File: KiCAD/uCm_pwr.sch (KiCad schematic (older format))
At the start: 31 parts, among them J1 5V_EXT, J2 3V3_EXT, P13 PWR_IN, P24 PWR_IN, U2 LM2675-5.0, U3 LM2675-3.3

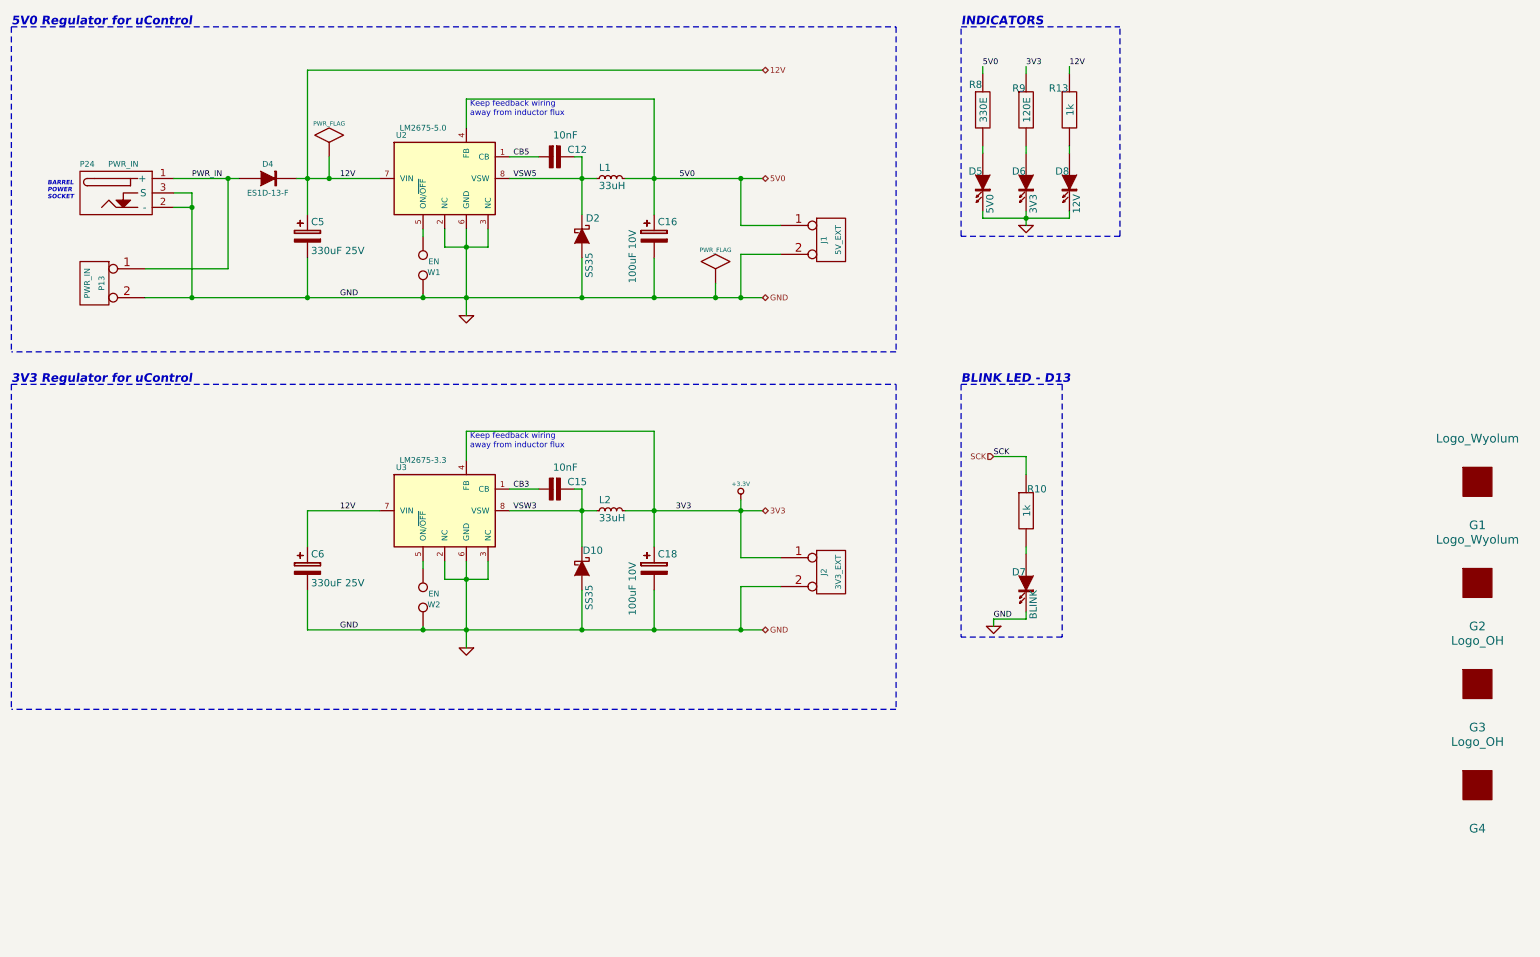
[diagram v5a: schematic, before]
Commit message: layout finalized, needs a check for errors
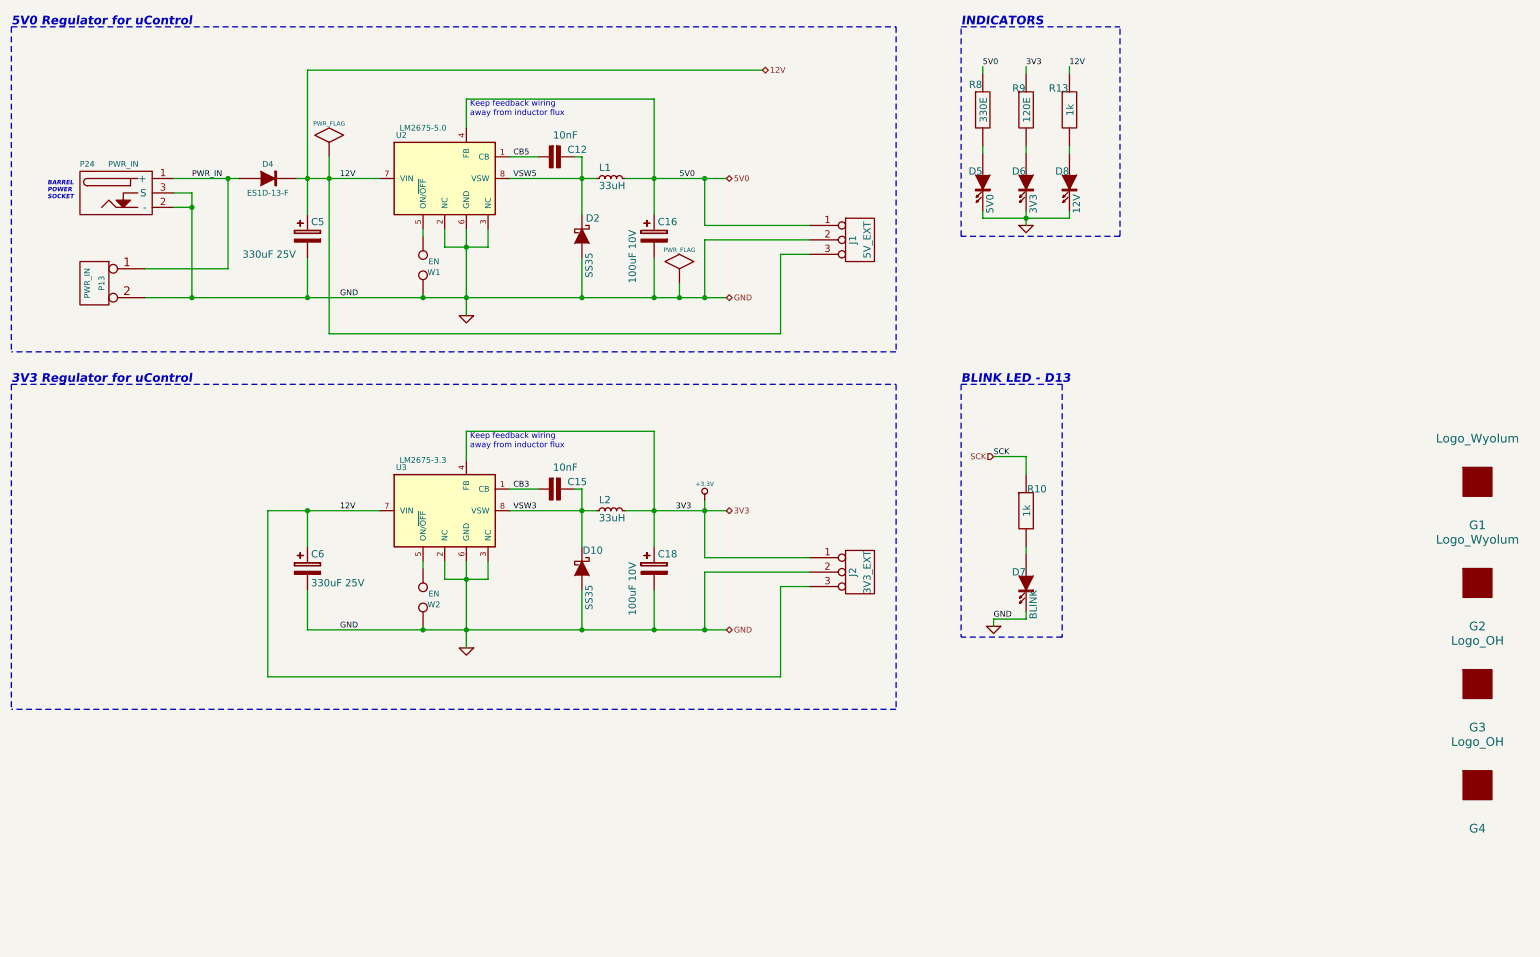
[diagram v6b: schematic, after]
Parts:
- removed J1: 5V_EXT, uCm:Header_2, symbol CONN_2
- removed J2: 3V3_EXT, uCm:Header_2, symbol CONN_2
- added J1: 5V_EXT, uCm:Header_3, symbol CONN_3
- added J2: 3V3_EXT, uCm:Header_3, symbol CONN_3
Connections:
- net +3.3V: now also J2.1 (P1)
- net 12V: now also J1.3 (P3), J2.3 (P3)
- net 5V0: now also J1.1 (P1)
- net GND: now also J1.2 (P2), J2.2 (P2)
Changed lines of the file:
@@
 Text Label 7925 875  0    40   ~ 0
 12V
-Text HLabel 5800 3950 2    40   BiDi ~ 0
+Text HLabel 5550 3950 2    40   BiDi ~ 0
 3V3
 $Comp
 L +3.3V #PWR012
 U 1 1 50DD3EAC
-P 5650 3875
-F 0 "#PWR012" H 5650 3835 30  0001 C CNN
-F 1 "+3.3V" H 5650 3985 30  0000 C CNN
-F 2 "" H 5650 3875 60  0001 C CNN
-F 3 "" H 5650 3875 60  0001 C CNN
-	1    5650 3875
+P 5400 3875
+F 0 "#PWR012" H 5400 3835 30  0001 C CNN
+F 1 "+3.3V" H 5400 3985 30  0000 C CNN
+F 2 "" H 5400 3875 60  0001 C CNN
+F 3 "" H 5400 3875 60  0001 C CNN
+	1    5400 3875
 	1    0    0    -1
 $EndComp
@@
 	-1   0    0    -1
 $EndComp
-$Comp
-L CONN_2 J1
-U 1 1 52ACA888
-P 6275 2075
-F 0 "J1" V 6225 2075 40  0000 C CNN
-F 1 "5V_EXT" V 6325 2075 40  0000 C CNN
-F 2 "uCm:Header_2" H 6275 1975 60  0001 C CNN
-F 3 "" H 6275 1975 60  0000 C CNN
-F 4 "PRPC002SFAN-RC" V 6275 2075 60  0001 C CNN "manf#"
-	1    6275 2075
-	1    0    0    -1
-$EndComp
 Wire Notes Line
 	600  3075 6725 3075
@@
 Text Notes 600  3075 0    60   Italic 12
 3V3 Regulator for uControl
-$Comp
-L CONN_2 J2
-U 1 1 52ACCF3E
-P 6275 4375
-F 0 "J2" V 6225 4375 40  0000 C CNN
-F 1 "3V3_EXT" V 6325 4375 40  0000 C CNN
-F 2 "uCm:Header_2" H 6275 4275 60  0001 C CNN
-F 3 "" H 6275 4275 60  0000 C CNN
-F 4 "PRPC002SFAN-RC" V 6275 4375 60  0001 C CNN "manf#"
-	1    6275 4375
-	1    0    0    -1
-$EndComp
 $Comp
 L LM2675-5.0 U2
@@
 	5050 1100 5050 1900
 Wire Wire Line
-	4850 1650 5800 1650
+	4850 1650 5550 1650
 Wire Wire Line
 	2650 900  2650 1900
@@
 	2650 2475 2650 2200
 Wire Wire Line
-	1525 2475 5800 2475
+	1525 2475 5550 2475
 Wire Wire Line
 	5050 2475 5050 2200
@@
 L PWR_FLAG #FLG016
 U 1 1 56649F69
-P 5475 2375
-F 0 "#FLG016" H 5475 2645 30  0001 C CNN
-F 1 "PWR_FLAG" H 5475 2605 30  0000 C CNN
-F 2 "" H 5475 2375 60  0000 C CNN
-F 3 "" H 5475 2375 60  0000 C CNN
-	1    5475 2375
+P 5225 2375
+F 0 "#FLG016" H 5225 2645 30  0001 C CNN
+F 1 "PWR_FLAG" H 5225 2605 30  0000 C CNN
+F 2 "" H 5225 2375 60  0000 C CNN
+F 3 "" H 5225 2375 60  0000 C CNN
+	1    5225 2375
 	1    0    0    -1
 $EndComp
 Text HLabel 5800 900  2    40   BiDi ~ 0
 12V
-Text HLabel 5800 2475 2    40   BiDi ~ 0
+Text HLabel 5550 2475 2    40   BiDi ~ 0
 GND
-Text HLabel 5800 1650 2    40   BiDi ~ 0
+Text HLabel 5550 1650 2    40   BiDi ~ 0
 5V0
 Wire Wire Line
@@
 Connection ~ 5050 2475
 Wire Wire Line
-	5475 2375 5475 2475
-Connection ~ 5475 2475
+	5225 2375 5225 2475
+Connection ~ 5225 2475
 Text Label 5225 1650 0    40   ~ 0
 5V0
 Wire Wire Line
-	5925 2175 5650 2175
-Wire Wire Line
-	5650 2175 5650 2475
-Connection ~ 5650 2475
-Wire Wire Line
-	5925 1975 5650 1975
-Wire Wire Line
-	5650 1975 5650 1650
-Connection ~ 5650 1650
+	6125 2075 5400 2075
+Wire Wire Line
+	5400 2075 5400 2475
+Connection ~ 5400 2475
+Wire Wire Line
+	6125 1975 5400 1975
+Wire Wire Line
+	5400 1975 5400 1650
+Connection ~ 5400 1650
 $Comp
 L GND #PWR017
@@
 	5050 3400 5050 4200
 Wire Wire Line
-	4850 3950 5800 3950
-Wire Wire Line
-	2650 3950 3150 3950
-Wire Wire Line
-	2650 4775 5800 4775
+	4850 3950 5550 3950
+Wire Wire Line
+	2375 3950 3150 3950
+Wire Wire Line
+	2650 4775 5550 4775
 Wire Wire Line
 	5050 4775 5050 4500
@@
 Text Label 2875 3950 0    40   ~ 0
 12V
-Text HLabel 5800 4775 2    40   BiDi ~ 0
+Text HLabel 5550 4775 2    40   BiDi ~ 0
 GND
 Connection ~ 5050 4775
 Wire Wire Line
-	5925 4475 5650 4475
-Wire Wire Line
-	5650 4475 5650 4775
-Connection ~ 5650 4775
-Wire Wire Line
-	5650 4275 5925 4275
-Wire Wire Line
-	5650 3875 5650 4275
-Connection ~ 5650 3950
+	6125 4375 5400 4375
+Wire Wire Line
+	5400 4375 5400 4775
+Connection ~ 5400 4775
+Wire Wire Line
+	5400 4275 6125 4275
+Wire Wire Line
+	5400 3875 5400 4275
+Connection ~ 5400 3950
 Text Label 5200 3950 0    40   ~ 0
 3V3
@@
 P 2650 2050
 F 0 "C5" H 2675 2150 50  0000 L CNN
-F 1 "330uF 25V" H 2675 1950 50  0000 L CNN
+F 1 "330uF 25V" H 2200 1925 50  0000 L CNN
 F 2 "uCm:C_ELCO_SMD_8x10" H 2688 1900 30  0001 C CNN
 F 3 "" H 2650 2050 60  0000 C CNN
@@
 $EndComp
 Wire Wire Line
-	2800 1500 2800 1650
+	2800 1500 2800 2725
 Connection ~ 2800 1650
+$Comp
+L CONN_3 J2
+U 1 1 5665ADBC
+P 6475 4375
+F 0 "J2" V 6425 4375 50  0000 C CNN
+F 1 "3V3_EXT" V 6525 4375 50  0000 C CNN
+F 2 "uCm:Header_3" H 6475 4375 60  0001 C CNN
+F 3 "" H 6475 4375 60  0000 C CNN
+F 4 "CONN HEADER 50POS .100\" SGL GOLD" H 6475 4475 60  0001 L CNN "Field4"
+F 5 "Header, Unshrouded, Male pin," H 6475 4575 60  0001 L CNN "Field5"
+F 6 "0.1\" pitch x 50 nos" H 6475 4675 60  0001 L CNN "Field6"
+F 7 "Samtec Inc" H 6475 4775 60  0001 L CNN "Field7"
+F 8 "TSW-150-07-L-S" H 6475 4875 60  0001 L CNN "Field8"
+F 9 "Digikey" H 6475 4975 60  0001 L CNN "Field9"
+F 10 "SAM1031-50-ND" H 6475 5075 60  0001 L CNN "Field10"
+F 11 "http://www.digikey.com/scripts/DkSearch/dksus.dll?WT.z_header=search_go&lang=en&keywords=SAM1031-50-ND&x=15&y=16&cur=USD" H 6475 5175 60  0001 L CNN "Field11"
+	1    6475 4375
+	1    0    0    -1
+$EndComp
+Wire Wire Line
+	2375 3950 2375 5100
+Wire Wire Line
+	2375 5100 5925 5100
+Wire Wire Line
+	5925 5100 5925 4475
+Wire Wire Line
+	5925 4475 6125 4475
+Connection ~ 2650 3950
+$Comp
+L CONN_3 J1
+U 1 1 5665B6DA
+P 6475 2075
+F 0 "J1" V 6425 2075 50  0000 C CNN
+F 1 "5V_EXT" V 6525 2075 50  0000 C CNN
+F 2 "uCm:Header_3" H 6475 2075 60  0001 C CNN
+F 3 "" H 6475 2075 60  0000 C CNN
+F 4 "CONN HEADER 50POS .100\" SGL GOLD" H 6475 2175 60  0001 L CNN "Field4"
+F 5 "Header, Unshrouded, Male pin," H 6475 2275 60  0001 L CNN "Field5"
+F 6 "0.1\" pitch x 50 nos" H 6475 2375 60  0001 L CNN "Field6"
+F 7 "Samtec Inc" H 6475 2475 60  0001 L CNN "Field7"
+F 8 "TSW-150-07-L-S" H 6475 2575 60  0001 L CNN "Field8"
+F 9 "Digikey" H 6475 2675 60  0001 L CNN "Field9"
+F 10 "SAM1031-50-ND" H 6475 2775 60  0001 L CNN "Field10"
+F 11 "http://www.digikey.com/scripts/DkSearch/dksus.dll?WT.z_header=search_go&lang=en&keywords=SAM1031-50-ND&x=15&y=16&cur=USD" H 6475 2875 60  0001 L CNN "Field11"
+	1    6475 2075
+	1    0    0    -1
+$EndComp
+Wire Wire Line
+	2800 2725 5925 2725
+Wire Wire Line
+	5925 2725 5925 2175
+Wire Wire Line
+	5925 2175 6125 2175
 $EndSCHEMATC
